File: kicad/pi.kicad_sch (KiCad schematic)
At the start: 9 parts, among them J2 Raspberry Pi

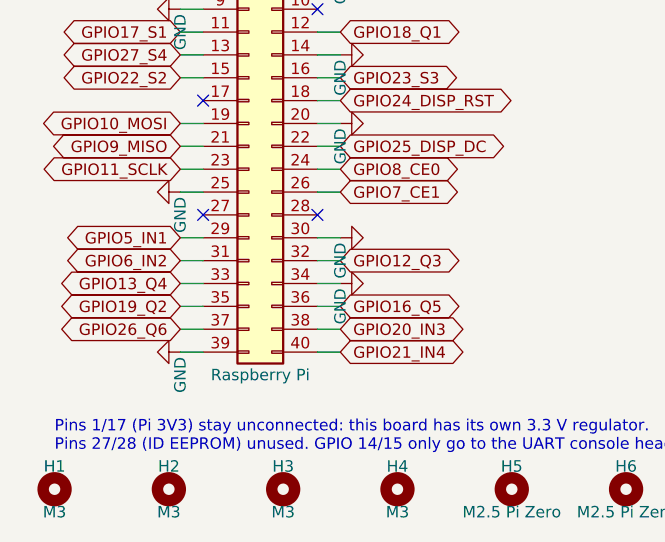
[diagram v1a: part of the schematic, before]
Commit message: kicad: reorder 74HCT244 channels for crossing-free Pi -> driver routing
Inputs enter U3 from outside (pull-downs R8..R13 as a staircase), outputs
leave inside under the IC body towards Q1..Q6. The GPIO order on the Pi
header then has to be Q6..Q1, so the stage mapping changes to
Q2 = GPIO12, Q3 = GPIO13, Q4 = GPIO19 (hardware PWM stays on GPIO18/19,
now Q1/Q4). Unused channels: pin 8/11 inputs to GND, pin 9/12 open.

Co-Authored-By: Claude Opus 5.5 <noreply@anthropic.com>
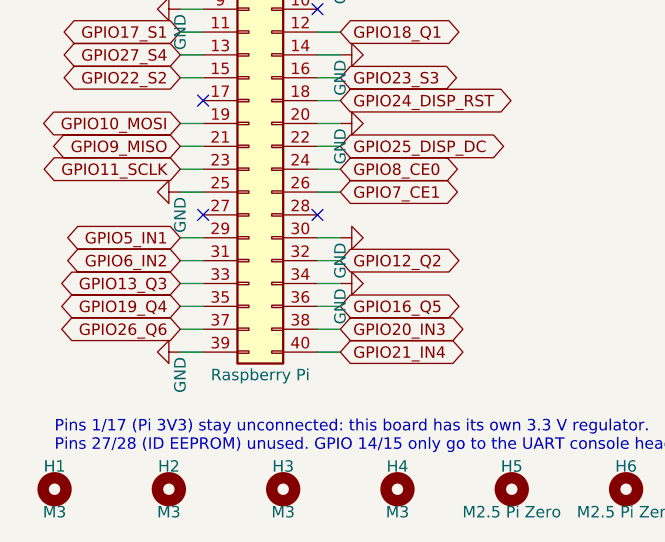
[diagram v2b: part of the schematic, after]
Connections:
- net GPIO12_Q3 renamed GPIO12_Q2
- net GPIO13_Q4 renamed GPIO13_Q3
- net GPIO19_Q2 renamed GPIO19_Q4
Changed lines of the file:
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@@
 		)
 	)
-	(global_label "GPIO13_Q4"
+	(global_label "GPIO13_Q3"
 		(shape bidirectional)
 		(at 39.37 81.28 180)
@@
 		)
 	)
-	(global_label "GPIO19_Q2"
+	(global_label "GPIO19_Q4"
 		(shape bidirectional)
 		(at 39.37 83.82 180)
@@
 		)
 	)
-	(global_label "GPIO12_Q3"
+	(global_label "GPIO12_Q2"
 		(shape bidirectional)
 		(at 57.15 78.74 0)

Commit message: kicad: drop Pi Zero holes next to the header, J19 value from board to schematic
H7/H8 and their standoff keep-outs removed: the box header no longer
collides with them (last DRC errors gone), the Zero's header side is held by
the plug connection and its outer side by H5/H6. J19 value "1-wire\nDS1820"
taken over from the board. README/BOM: 2 standoffs instead of 4.

Co-Authored-By: Claude Opus 5.5 <noreply@anthropic.com>
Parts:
- removed H7, H8: M2.5 Pi Zero, MountingHole:MountingHole_2.7mm_M2.5, symbol Mechanical:MountingHole
